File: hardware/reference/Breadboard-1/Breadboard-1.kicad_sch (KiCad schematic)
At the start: 68 parts, among them J1 01x06, J2 01x06, J3 01x05, J4 01x07, J5 01x05S, Q31 2N7002, Q51 SL2309, Q52 SL2309, Q53 DTC143ZCA, Q54 DTC143ZCA, Q55 DMN6140, Q56 DMN6140, Q71 2N7002, Q72 2N7002, Q73 2N7002, Q74 2N7002, Q75 2N7002, Q76 2N7002, U11 ME6203A, U21 PIC18F16Q40

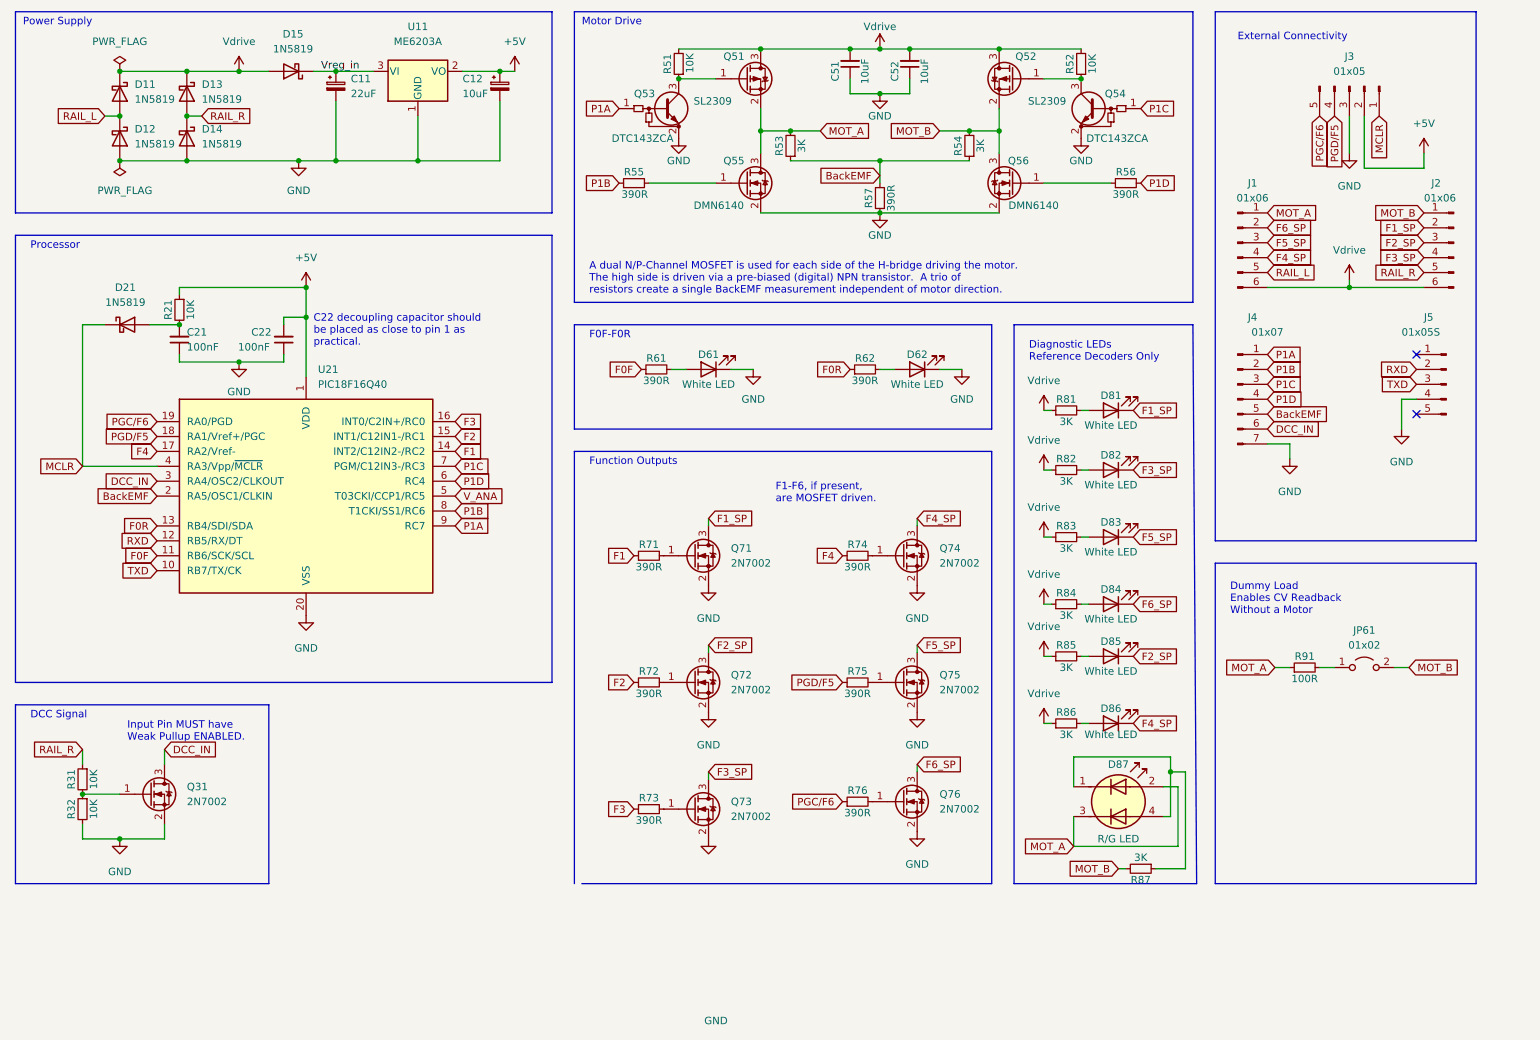
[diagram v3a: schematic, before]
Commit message: Switched regulator, added "super capacitor" location.
Switched the linear regulator to a SE8633X2-HF which has superior
performance characteristics.  Switched back to 0805 10uF resistors
as a result.  Reworked regulator area, using copper fills to lower
resistance between components per data sheet recomendation.

Added C11, a spot for an electrolytic "super capacitor" of up to 1000uF
to help smooth out input electrical issues.  Moved a few traces to make
space for it.

Updated CALCULATIONS.xlsx to match.  Regenerated .jpg and .pdf.
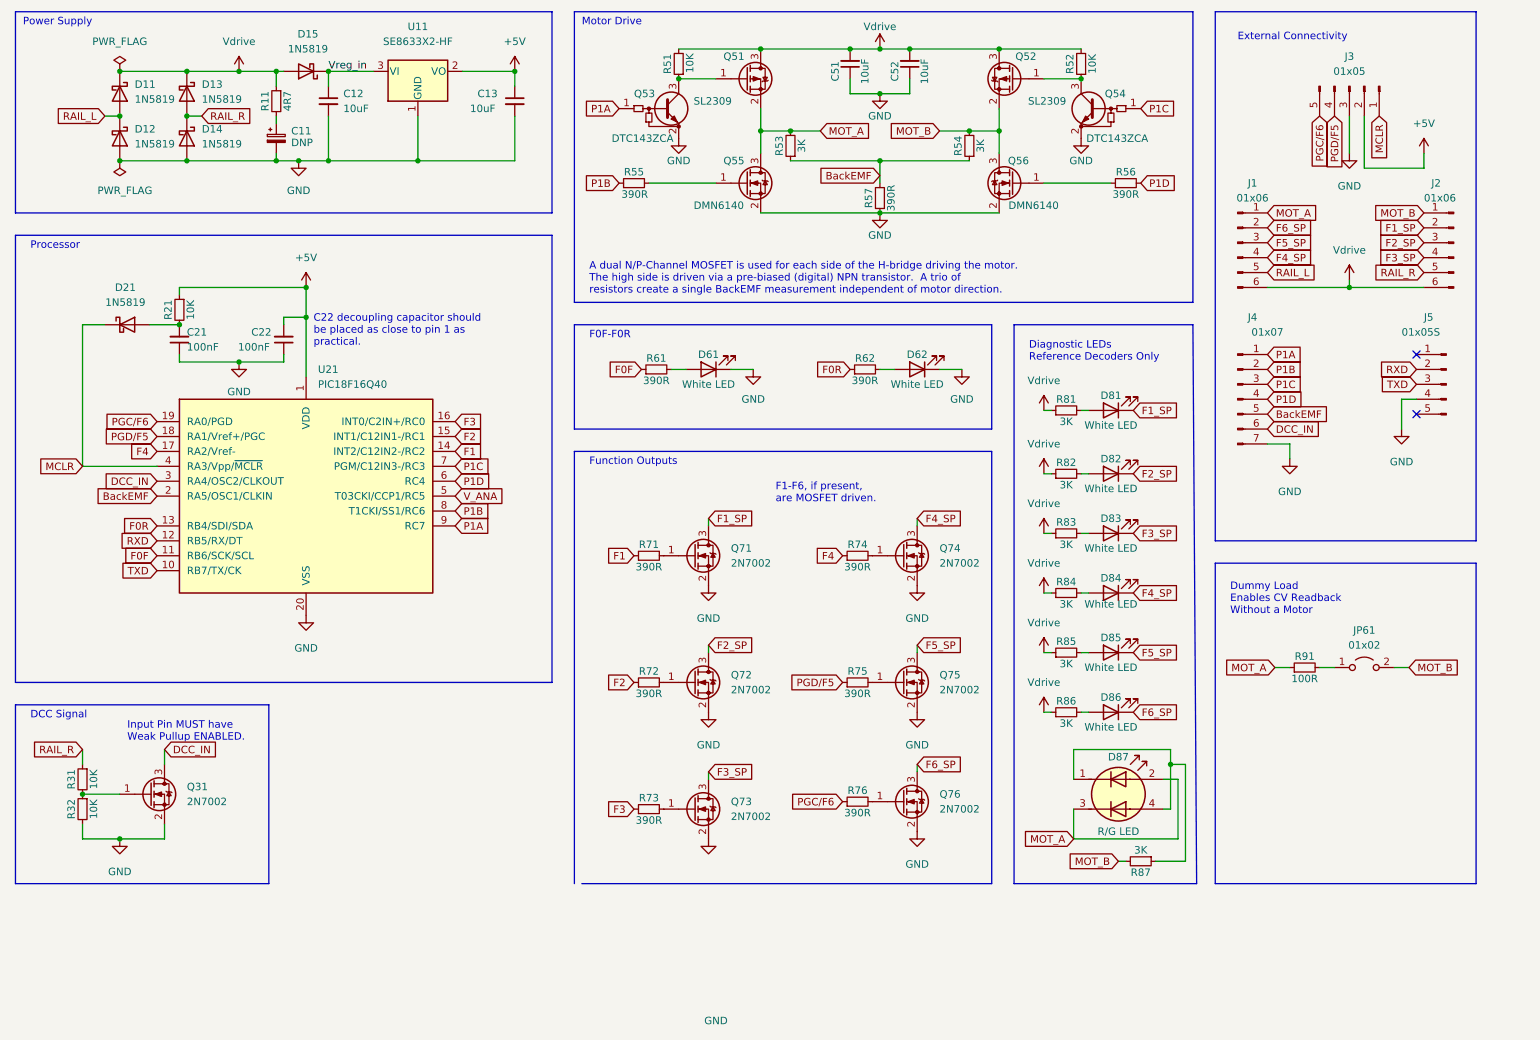
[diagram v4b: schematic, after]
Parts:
- removed C12: 10uF, Capacitor_Tantalum_SMD:CP_EIA-3216-18_Kemet-A, symbol Device:C_Polarized_Small
- added C11: DNP, Capacitor_THT:CP_Radial_D10.0mm_P2.50mm_P5.00mm, symbol Device:C_Polarized_Small
- added C13: 10uF, Capacitor_SMD:C_0805_2012Metric, symbol Device:C_Small
- added R11: 4R7, Resistor_SMD:R_0805_2012Metric, symbol Device:R_Small
- C12: renamed from C11; value 22uF -> 10uF; footprint Capacitor_Tantalum_SMD:CP_EIA-7343-31_Kemet-D -> Capacitor_SMD:C_0805_2012Metric; symbol Device:C_Polarized_Small -> Device:C_Small; Cost 0.43 -> 0.01; LCSC C7225 -> C440198; MPN TAJD226K035RNJ -> Generic; Specification CASE-D-7343 35V 22uF Tantalum 10% -> 0805 50V 10uF X5R 10%
- U11: value ME6203A -> SE8633X2-HF; Cost 0.08 -> 0.13; LCSC C87842 -> C496613; MPN ME6203A33M3G -> SE8633X2-HF; Specification SOT-23 100ma 40V to 3.3V LDO -> SOT-23 200mA Fixed 3.3V 80VLDO
- renumbered D85 to D82, D82 to D83, D86 to D84, D83 to D85, D84 to D86, R85 to R82, R82 to R83, R86 to R84, R83 to R85, R84 to R86
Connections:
- net +5V: now also C13.1
- net GND: now also C11.2, C13.2
- net Vdrive: now also R11.1
- new net: C11.1, R11.2
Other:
- moved on the sheet: D15, D82, D83, D84, D85, D86, D87, R82, R83, R84, R85, R86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

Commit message: Plot paramters to get good gerbers.
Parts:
- C11: Specification Location for user-supplied "super capacitor", up to D10 and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 -> Location for user-supplied super capacitor up to D10 and Pi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
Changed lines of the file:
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@@
       (effects (font (size 1.27 1.27)) hide)
     )
-    (property "Specification" "Location for user-supplied \"super capacitor\", up to D10 and Pitch of 2.5 or 5mm." (id 7) (at 59.69 36.83 0)
+    (property "Specification" "Location for user-supplied super capacitor up to D10 and Pitch of 2.5 or 5mm." (id 7) (at 59.69 36.83 0)
       (effects (font (size 1.27 1.27)) hide)
     )

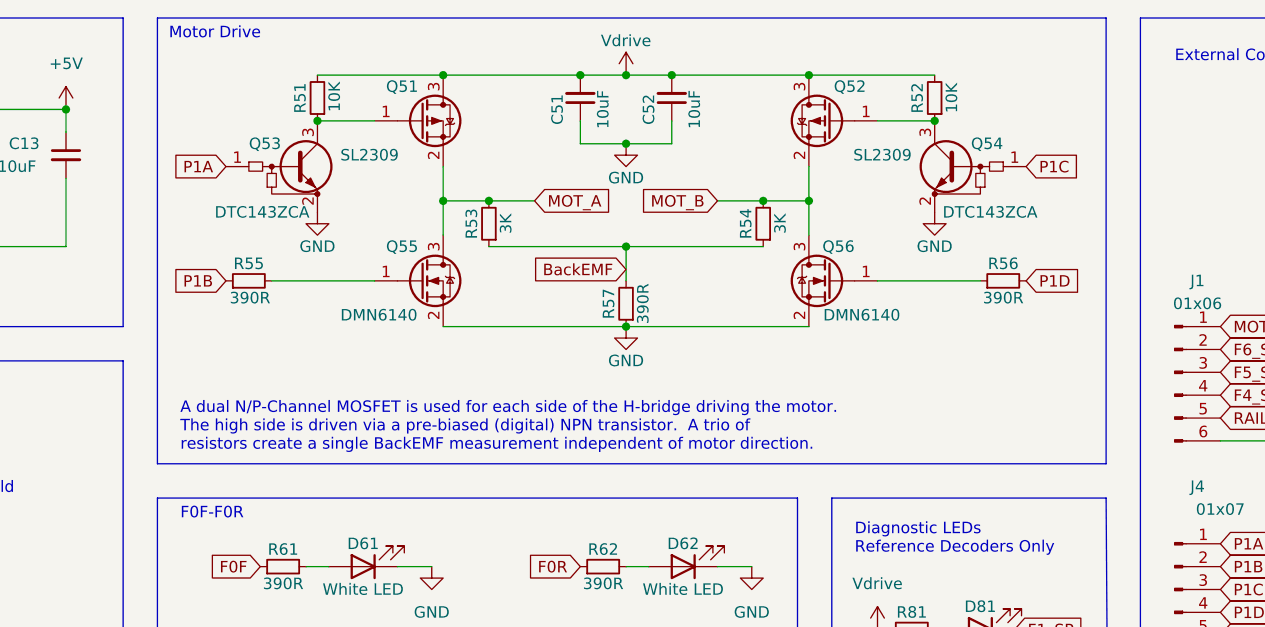
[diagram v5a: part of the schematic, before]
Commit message: Correct over-voltage on high side drive.
The P-Channel MOSFET gate would be driven to 0v by the old driver
circuit.  When the DCC voltage is > 20v, this exceeds the Vgs
maximum of the part.

Added another resistor to make a voltage divider cutting the voltage
in half, and thus driving the gate at 15v when Vdrive is 30v.  Now
Vgs is always within range of the part.
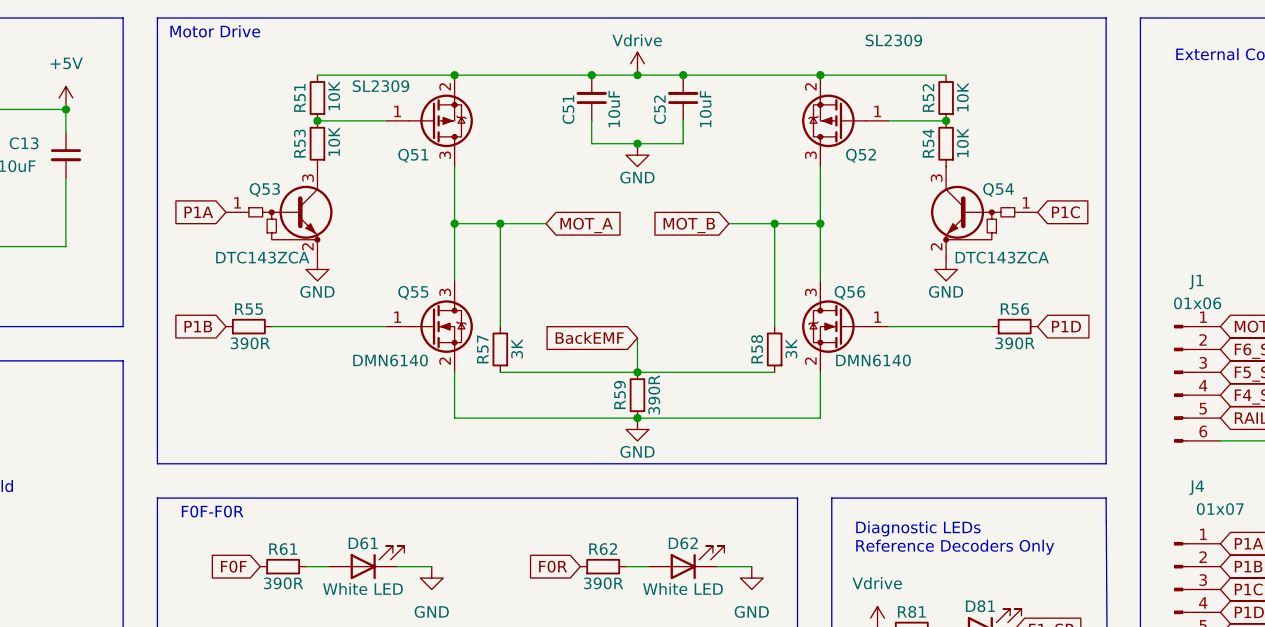
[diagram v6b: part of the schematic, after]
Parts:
- added R53, R54: 10K, Resistor_SMD:R_0805_2012Metric, symbol Device:R_Small
- renumbered R53 to R57, R54 to R58, R57 to R59
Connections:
- net MOT_A: now also Q51.3 (D); no longer Q51.2 (S)
- net MOT_B: now also Q52.3 (D); no longer Q52.2 (S)
- net Vdrive: now also Q51.2 (S), Q52.2 (S); no longer Q51.3 (D), Q52.3 (D)
- net at Q51.1 (G), R51.1: now also R53.2; no longer Q53.3 (C)
- net at Q52.1 (G), R52.1: now also R54.2; no longer Q54.3 (C)
- new net: Q54.3 (C), R54.1
- new net: Q53.3 (C), R53.1
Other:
- note removed: "A dual N/P-Channel MOSFET is used for each side of the H-bridge driving the motor. The high side is driven via a pre-biased (digital) NPN transistor. A trio of resistors create a single BackEMF measurement independent of motor direction."
- moved on the sheet: C51, C52, Q51, Q52, Q53, Q54, Q55, Q56, R52, R55, R56, R57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

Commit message: Clarity improvements.
1) Moved the dummy load block on the schematic so the external connectivity
   block could be larger.  This enables desgins that need more external
   connectivity (e.g. Wired-Altas-1A-2) to use the same schematic layout.

2) Updated CALCULATIONS tab numbering to include component numbers in that
   block.

3) Updated CALCULATIONS for the motor driver to include a discussion about
   gate resistor selection and gate driving timers.
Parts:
- renumbered JP61 to JP41, R91 to R41
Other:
- moved on the sheet: JP41, R41, R55, R56

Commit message: Updated MOSFETS to be ESD protected versions.  Updated calculations.
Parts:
- Q31, Q71, Q72, Q73, Q74, Q75, Q76: value 2N7002 -> BSS138K; Cost 0.01 -> 0.012; LCSC C8545 -> C5224263; MPN 2N7002 -> BSS138K; Specification SOT-23 60V 340mA 0.9Ω@10V,500mA 0.35W 1.3V@1mA N Channel -> SOT-23 50V 300mA 1.5Ω@10V,500mA 300mW N Channel
- Q51, Q52: value SL2309 -> PMV250EPEA; Cost 0.04 -> 0.12; LCSC C2843304 -> C477997; MPN SL2309 -> PMV250EPEA; Specification SOT-23 60V 1.6A 140mΩ@10V,1.5A 1.5W 2V@250uA P Channel -> SOT-23 40V 1.5A 240mΩ@1.3A,10V P Channel
- Q55, Q56: value DMN6140 -> PMV55ENEAR; Cost 0.08 -> 0.20; LCSC C211403 -> C294616; MPN DMN6140 -> PMV55ENEAR; Specification SOT-23 60V 1.6A 140mΩ@10V,1.8A 700mW 3V@250uA N Channel -> SOT-23 60V 3.1A 60mΩ@10V,3.1A N Channel
- R31: value 10K -> 390R; LCSC C17414 -> C17655; Specification 0805 10K Ω 1% 1/8W -> 0805 390 Ω 1% 1/8W
- R57, R58: value 3K -> 22K; LCSC C17661 -> C17560; Specification 0805 3K Ω 1% 1/8W -> 0805 22K Ω 1% 1/8W
- R59: value 390R -> 3K; LCSC C17655 -> C17661; Specification 0805 390 Ω 1% 1/8W -> 0805 3K Ω 1% 1/8W
